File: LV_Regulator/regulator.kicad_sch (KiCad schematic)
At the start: 41 parts, among them U5 BQ25858QWRRVRQ1, U6 CSD19506KTT, U7 CSD19506KTT, U8 CSD19506KTT, U9 CSD19506KTT

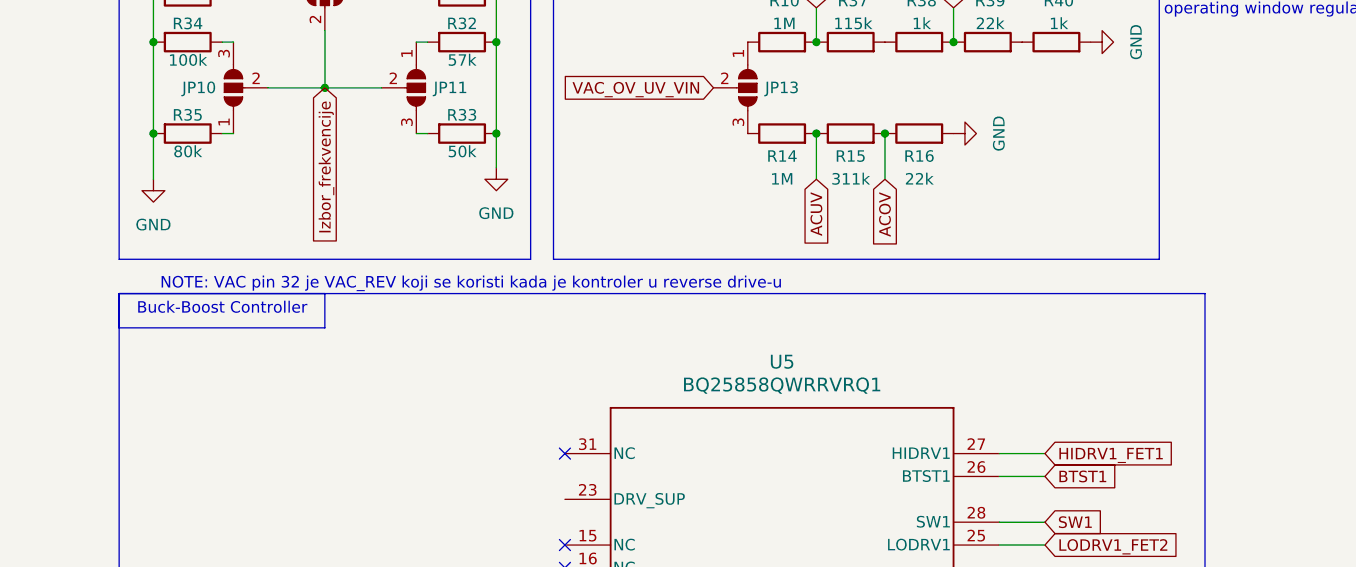
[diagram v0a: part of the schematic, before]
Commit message: Updated Note for Regulator
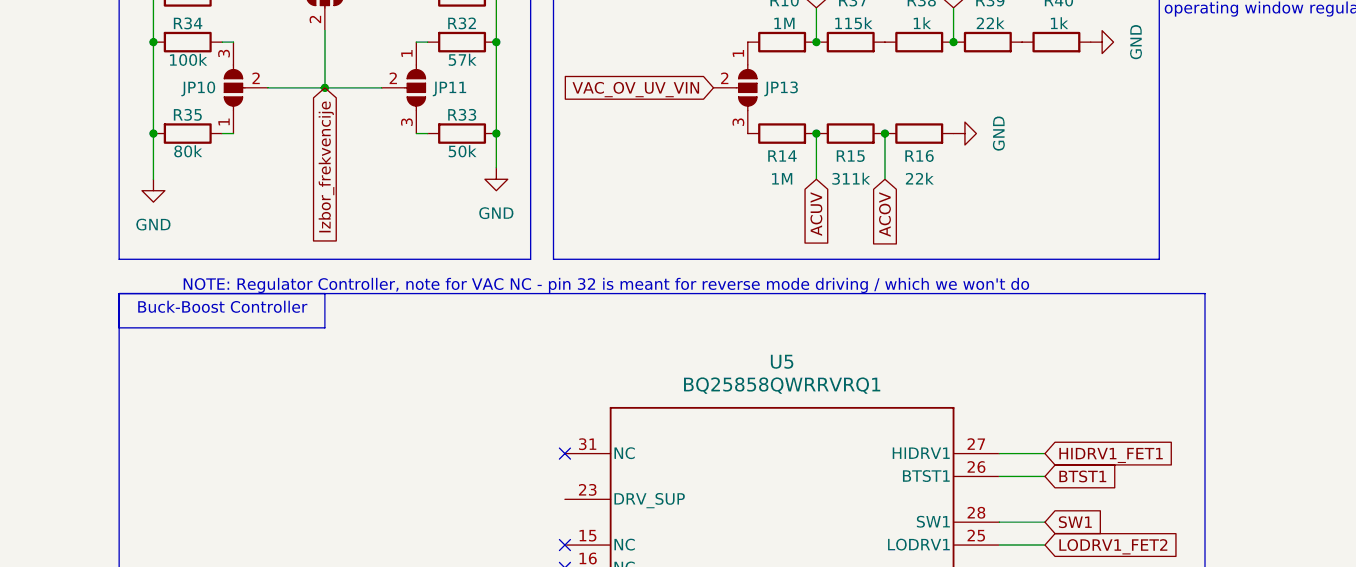
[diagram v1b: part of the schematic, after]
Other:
- note added: "NOTE: Regulator Controller, note for VAC NC - pin 32 is meant for reverse mode driving / which we won't do"
- note removed: "NOTE: VAC pin 32 je VAC_REV koji se koristi kada je kontroler u reverse drive-u"
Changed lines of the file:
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@@
 		)
 	)
-	(text "NOTE: VAC pin 32 je VAC_REV koji se koristi kada je kontroler u reverse drive-u\n"
+	(text "NOTE: Regulator Controller, note for VAC NC - pin 32 is meant for reverse mode driving / which we won't do\n"
 		(exclude_from_sim no)
-		(at 51.816 52.324 0)
+		(at 66.802 52.578 0)
 		(effects
 			(font

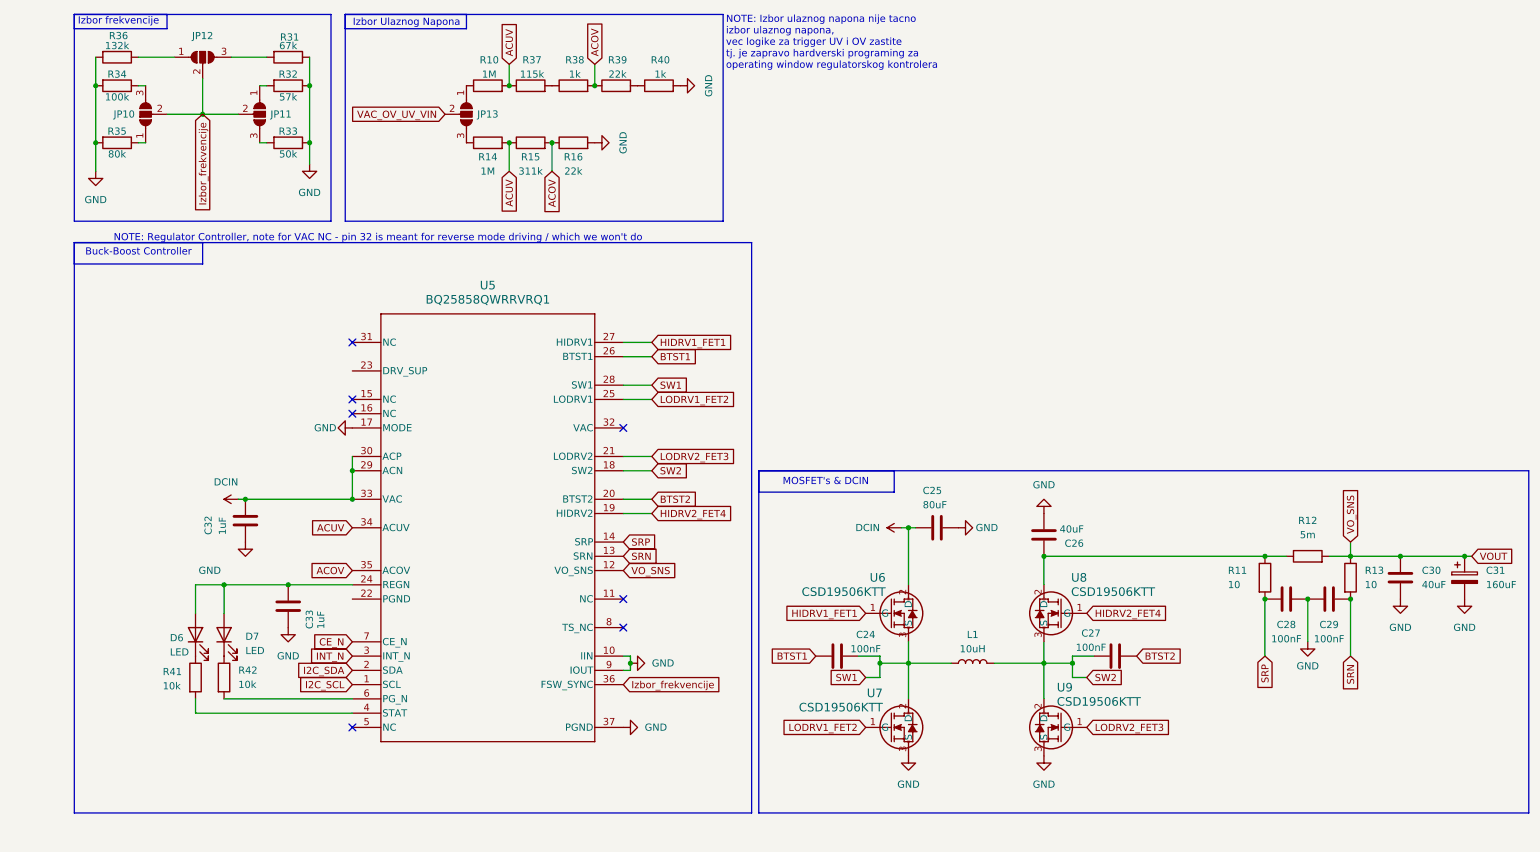
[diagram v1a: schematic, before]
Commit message: Regulator Update & MCU pins
Update schematic and connected Regulator to MCU
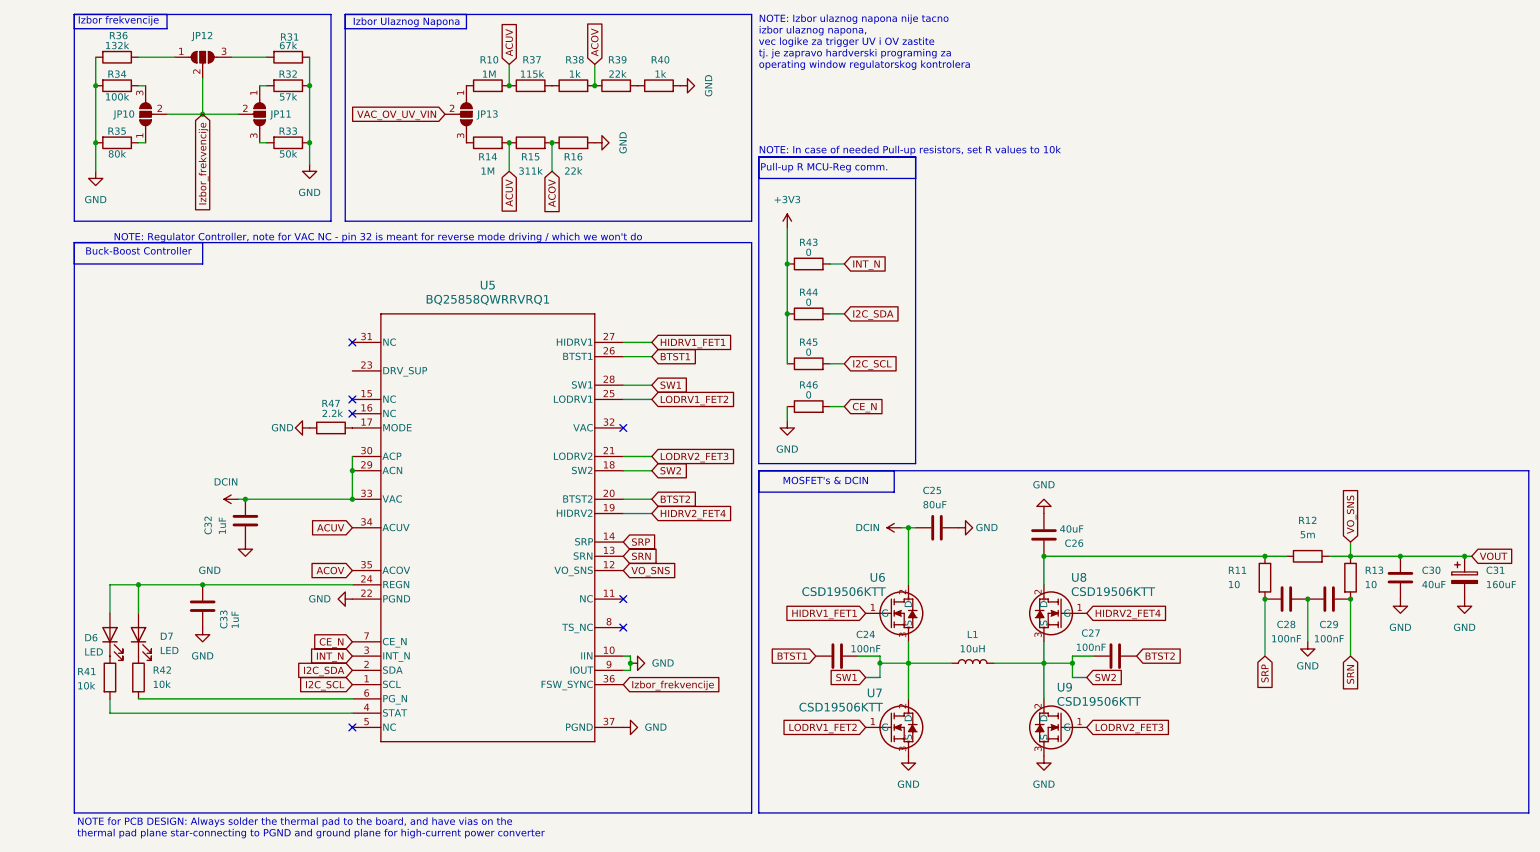
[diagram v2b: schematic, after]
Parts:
- added R43, R44, R45, R46: 0, symbol Device:R
- added R47: 2.2k, symbol Device:R
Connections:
- net CE_N: now also R46.2
- net GND: now also U5.22 (PGND), R46.1, R47.1; no longer U5.17 (MODE)
- net I2C_SCL: now also R45.2
- net I2C_SDA: now also R44.2
- net INT_N: now also R43.2
- new net: R47.2, U5.17 (MODE)
- new net +3V3: R43.1, R44.1, R45.1
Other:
- note added: "NOTE for PCB DESIGN: Always solder the thermal pad to the board, and have vias on the thermal pad plane star-connecting to PGND and ground plane for high-current power converter"
- note added: "NOTE: In case of needed Pull-up resistors, set R values to 10k"
- note added: "Pull-up R MCU-Reg comm."
- moved on the sheet: C33, D6, D7, R41, R42

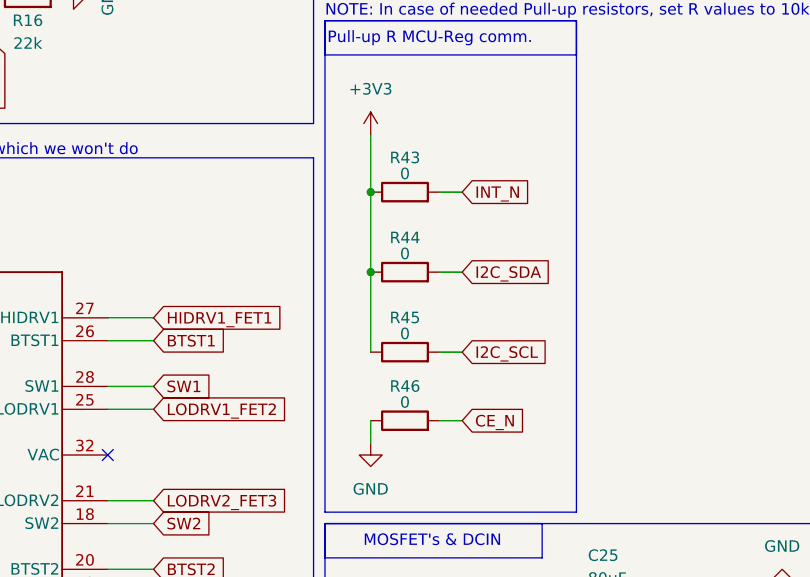
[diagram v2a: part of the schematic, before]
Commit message: Update regulator.kicad_sch
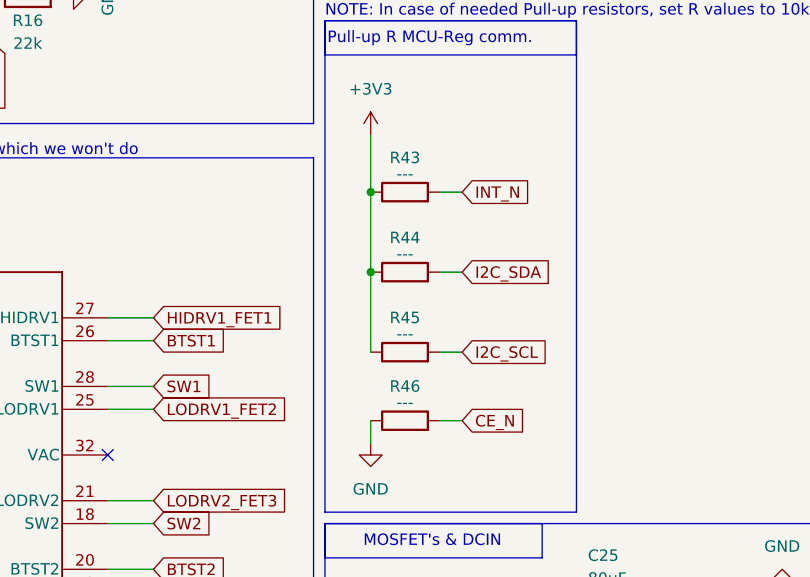
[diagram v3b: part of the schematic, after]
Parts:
- R43, R44, R45, R46: value 0 -> ---
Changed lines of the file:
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@@
 			)
 		)
-		(property "Value" "0"
+		(property "Value" "---"
 			(at 143.51 72.898 90)
 			(effects
@@
 			)
 		)
-		(property "Value" "0"
+		(property "Value" "---"
 			(at 143.51 64.008 90)
 			(effects
@@
 			)
 		)
-		(property "Value" "0"
+		(property "Value" "---"
 			(at 143.51 80.518 90)
 			(effects
@@
 			)
 		)
-		(property "Value" "0"
+		(property "Value" "---"
 			(at 143.51 55.118 90)
 			(effects

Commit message: added certain footprints
Added footprints for certain parts such as the BQ25858Q1 regulator controller & CSD19506 MOSFET for PCB design and put in footprints (will need change)
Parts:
- C24, C25, C26, C27, C28, C29, C30, C32, C33: footprint (none) -> Capacitor_SMD:C_1206_3216Metric
- D6, D7: footprint (none) -> Diode_SMD:D_1206_3216Metric_Pad1.42x1.75mm_HandSolder
- JP10, JP11, JP12, JP13: footprint (none) -> Jumper:SolderJumper-3_P1.3mm_Open_Pad1.0x1.5mm
- L1: footprint (none) -> Inductor_SMD:L_APV_APH1770
- R10, R11, R12, R13, R14, R15, R16, R31, R32, R33, R34, R35, R36, R37, R38, R39, R40, R41, R42, R43, R44, R45, R46, R47: footprint (none) -> Resistor_SMD:R_1206_3216Metric
- U5: footprint RRV0036B-IPC_A -> ul_BQ25858QWRRVRQ1:RRV0036B-IPC_A
- U6, U7, U8, U9: footprint DDPAK/TO-263_KTT_TEX -> CSD19506KTT:DDPAK&slash_TO-263_KTT_TEX
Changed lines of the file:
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@@
 			)
 		)
-		(property "Footprint" ""
+		(property "Footprint" "Resistor_SMD:R_1206_3216Metric"
 			(at 143.51 76.708 90)
 			(effects
@@
 			)
 		)
-		(property "Footprint" ""
+		(property "Footprint" "Resistor_SMD:R_1206_3216Metric"
 			(at 17.272 130.81 90)
 			(effects
@@
 			)
 		)
-		(property "Footprint" ""
+		(property "Footprint" "Resistor_SMD:R_1206_3216Metric"
 			(at 101.6 27.178 90)
 			(effects
@@
 			)
 		)
-		(property "Footprint" ""
+		(property "Footprint" "Resistor_SMD:R_1206_3216Metric"
 			(at 58.42 88.138 90)
 			(effects
@@
 			)
 		)
-		(property "Footprint" ""
+		(property "Footprint" "Diode_SMD:D_1206_3216Metric_Pad1.42x1.75mm_HandSolder"
 			(at 19.05 123.19 0)
 			(effects
@@
 			)
 		)
-		(property "Footprint" ""
+		(property "Footprint" "Capacitor_SMD:C_1206_3216Metric"
 			(at 184.4548 101.6 0)
 			(effects
@@
 			)
 		)
-		(property "Footprint" ""
+		(property "Footprint" "Resistor_SMD:R_1206_3216Metric"
 			(at 143.51 67.818 90)
 			(effects
@@
 			)
 		)
-		(property "Footprint" ""
+		(property "Footprint" "Resistor_SMD:R_1206_3216Metric"
 			(at 20.32 33.782 90)
 			(effects
@@
 			)
 		)
-		(property "Footprint" ""
+		(property "Footprint" "Resistor_SMD:R_1206_3216Metric"
 			(at 22.352 130.81 90)
 			(effects
@@
 			)
 		)
-		(property "Footprint" "DDPAK/TO-263_KTT_TEX"
+		(property "Footprint" "CSD19506KTT:DDPAK&slash_TO-263_KTT_TEX"
 			(at 153.67 139.7 0)
 			(effects
@@
 			)
 		)
-		(property "Footprint" ""
+		(property "Footprint" "Resistor_SMD:R_1206_3216Metric"
 			(at 232.41 110.998 90)
 			(effects
@@
 			)
 		)
-		(property "Footprint" ""
+		(property "Footprint" "Resistor_SMD:R_1206_3216Metric"
 			(at 116.84 27.178 90)
 			(effects
@@
 			)
 		)
-		(property "Footprint" ""
+		(property "Footprint" "Capacitor_SMD:C_1206_3216Metric"
 			(at 42.2148 99.06 0)
 			(effects
@@
 			)
 		)
-		(property "Footprint" ""
+		(property "Footprint" "Resistor_SMD:R_1206_3216Metric"
 			(at 50.8 18.542 90)
 			(effects
@@
 			)
 		)
-		(property "Footprint" ""
+		(property "Footprint" "Capacitor_SMD:C_1206_3216Metric"
 			(at 170.18 103.1748 0)
 			(effects
@@
 			)
 		)
-		(property "Footprint" ""
+		(property "Footprint" "Jumper:SolderJumper-3_P1.3mm_Open_Pad1.0x1.5mm"
 			(at 25.4 30.48 0)
 			(effects
@@
 			)
 		)
-		(property "Footprint" "DDPAK/TO-263_KTT_TEX"
+		(property "Footprint" "CSD19506KTT:DDPAK&slash_TO-263_KTT_TEX"
 			(at 193.04 119.38 0)
 			(effects
@@
 			)
 		)
-		(property "Footprint" ""
+		(property "Footprint" "Resistor_SMD:R_1206_3216Metric"
 			(at 20.32 23.622 90)
 			(effects
@@
 			)
 		)
-		(property "Footprint" ""
+		(property "Footprint" "Resistor_SMD:R_1206_3216Metric"
 			(at 101.6 37.338 90)
 			(effects
@@
 			)
 		)
-		(property "Footprint" ""
+		(property "Footprint" "Resistor_SMD:R_1206_3216Metric"
 			(at 50.8 33.782 90)
 			(effects
@@
 			)
 		)
-		(property "Footprint" ""
+		(property "Footprint" "Capacitor_SMD:C_1206_3216Metric"
 			(at 194.31 127.9652 0)
 			(effects
@@
 			)
 		)
-		(property "Footprint" "DDPAK/TO-263_KTT_TEX"
+		(property "Footprint" "CSD19506KTT:DDPAK&slash_TO-263_KTT_TEX"
 			(at 193.04 139.7 0)
 			(effects
@@
 			)
 		)
-		(property "Footprint" ""
+		(property "Footprint" "Resistor_SMD:R_1206_3216Metric"
 			(at 50.8 23.622 90)
 			(effects
@@
 		(on_board yes)
 		(dnp no)
-		(fields_autoplaced yes)
 		(property "Reference" "U5"
 			(at 86.36 60.96 0)
@@
 			)
 		)
-		(property "Footprint" "RRV0036B-IPC_A"
+		(property "Footprint" "ul_BQ25858QWRRVRQ1:RRV0036B-IPC_A"
 			(at 62.23 71.12 0)
 			(effects
@@
 			)
 		)
-		(property "Footprint" ""
+		(property "Footprint" "Diode_SMD:D_1206_3216Metric_Pad1.42x1.75mm_HandSolder"
 			(at 24.13 123.19 0)
 			(effects
@@
 			)
 		)
-		(property "Footprint" ""
+		(property "Footprint" "Capacitor_SMD:C_1206_3216Metric"
 			(at 152.4 126.0348 0)
 			(effects
@@
 			)
 		)
-		(property "Footprint" ""
+		(property "Footprint" "Capacitor_SMD:C_1206_3216Metric"
 			(at 34.5948 114.3 0)
 			(effects
@@
 			)
 		)
-		(property "Footprint" ""
+		(property "Footprint" "Inductor_SMD:L_APV_APH1770"
 			(at 172.72 128.27 0)
 			(effects
@@
 			)
 		)
-		(property "Footprint" ""
+		(property "Footprint" "Resistor_SMD:R_1206_3216Metric"
 			(at 86.36 37.338 90)
 			(effects
@@
 			)
 		)
-		(property "Footprint" ""
+		(property "Footprint" "Resistor_SMD:R_1206_3216Metric"
 			(at 223.012 113.03 90)
 			(effects
@@
 			)
 		)
-		(property "Footprint" ""
+		(property "Footprint" "Capacitor_SMD:C_1206_3216Metric"
 			(at 249.8852 116.84 0)
 			(effects
@@
 			)
 		)
-		(property "Footprint" ""
+		(property "Footprint" "Resistor_SMD:R_1206_3216Metric"
 			(at 86.36 27.178 90)
 			(effects
@@
 			)
 		)
-		(property "Footprint" ""
+		(property "Footprint" "Resistor_SMD:R_1206_3216Metric"
 			(at 109.22 27.178 90)
 			(effects
@@
 			)
 		)
-		(property "Footprint" ""
+		(property "Footprint" "Capacitor_SMD:C_1206_3216Metric"
 			(at 232.41 115.8748 0)
 			(effects
@@
 			)
 		)
-		(property "Footprint" ""
+		(property "Footprint" "Resistor_SMD:R_1206_3216Metric"
 			(at 93.98 37.338 90)
 			(effects
@@
 			)
 		)
-		(property "Footprint" ""
+		(property "Footprint" "Resistor_SMD:R_1206_3216Metric"
 			(at 238.252 113.03 90)
 			(effects
@@
 			)
 		)
-		(property "Footprint" ""
+		(property "Footprint" "Resistor_SMD:R_1206_3216Metric"
 			(at 20.32 18.542 90)
 			(effects
@@
 			)
 		)
-		(property "Footprint" ""
+		(property "Footprint" "Jumper:SolderJumper-3_P1.3mm_Open_Pad1.0x1.5mm"
 			(at 35.56 20.32 0)
 			(effects
@@
 			)
 		)
-		(property "Footprint" ""
+		(property "Footprint" "Capacitor_SMD:C_1206_3216Metric"
 			(at 240.03 115.8748 0)
 			(effects
@@
 			)
 		)
-		(property "Footprint" ""
+		(property "Footprint" "Resistor_SMD:R_1206_3216Metric"
 			(at 93.98 27.178 90)
 			(effects
@@
 			)
 		)
-		(property "Footprint" ""
+		(property "Footprint" "Resistor_SMD:R_1206_3216Metric"
 			(at 143.51 84.328 90)
 			(effects
@@
 			)
 		)
-		(property "Footprint" ""
+		(property "Footprint" "Resistor_SMD:R_1206_3216Metric"
 			(at 143.51 58.928 90)
 			(effects
@@
 			)
 		)
-		(property "Footprint" "DDPAK/TO-263_KTT_TEX"
+		(property "Footprint" "CSD19506KTT:DDPAK&slash_TO-263_KTT_TEX"
 			(at 153.67 119.38 0)
 			(effects
@@
 			)
 		)
-		(property "Footprint" ""
+		(property "Footprint" "Jumper:SolderJumper-3_P1.3mm_Open_Pad1.0x1.5mm"
 			(at 82.55 30.48 0)
 			(effects
@@
 			)
 		)
-		(property "Footprint" ""
+		(property "Footprint" "Jumper:SolderJumper-3_P1.3mm_Open_Pad1.0x1.5mm"
 			(at 45.72 30.48 0)
 			(effects

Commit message: Multiple Footprints Added
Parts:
- C31: footprint (none) -> ul_UCZ1J181MNQ1MS:CAP_UCD_12P5X13P5_NCH
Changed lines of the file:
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@@
 			)
 		)
-		(property "Footprint" ""
+		(property "Footprint" "ul_UCZ1J181MNQ1MS:CAP_UCD_12P5X13P5_NCH"
 			(at 261.3152 116.84 0)
 			(effects
